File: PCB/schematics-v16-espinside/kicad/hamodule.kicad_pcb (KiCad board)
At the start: 2 copper layers, 76.7 x 84.3 mm, 77 parts, among them J1 2604-1104, J2 2604-1102, J3 USB_B_Micro, J4 ESP Relays, J5 Current Jumper, J6 GND 3.3V, J7 Conn_01x02, J8 Current Jumper, J9 2604-1104, K1 PCN-105D, K2 PCN-105D, K3 PCN-105D, K4 PCN-105D, Q1 2N2219, Q2 2N2219, SW1 EN, SW2 IO0, U1 ULN2003A, U2 ESP32-WROOM-32D, U3 CP2102N-A01-GQFN24, U4 LD1117AV33_TO220, U6 LDA210-PDIP, U7 LDA210-PDIP

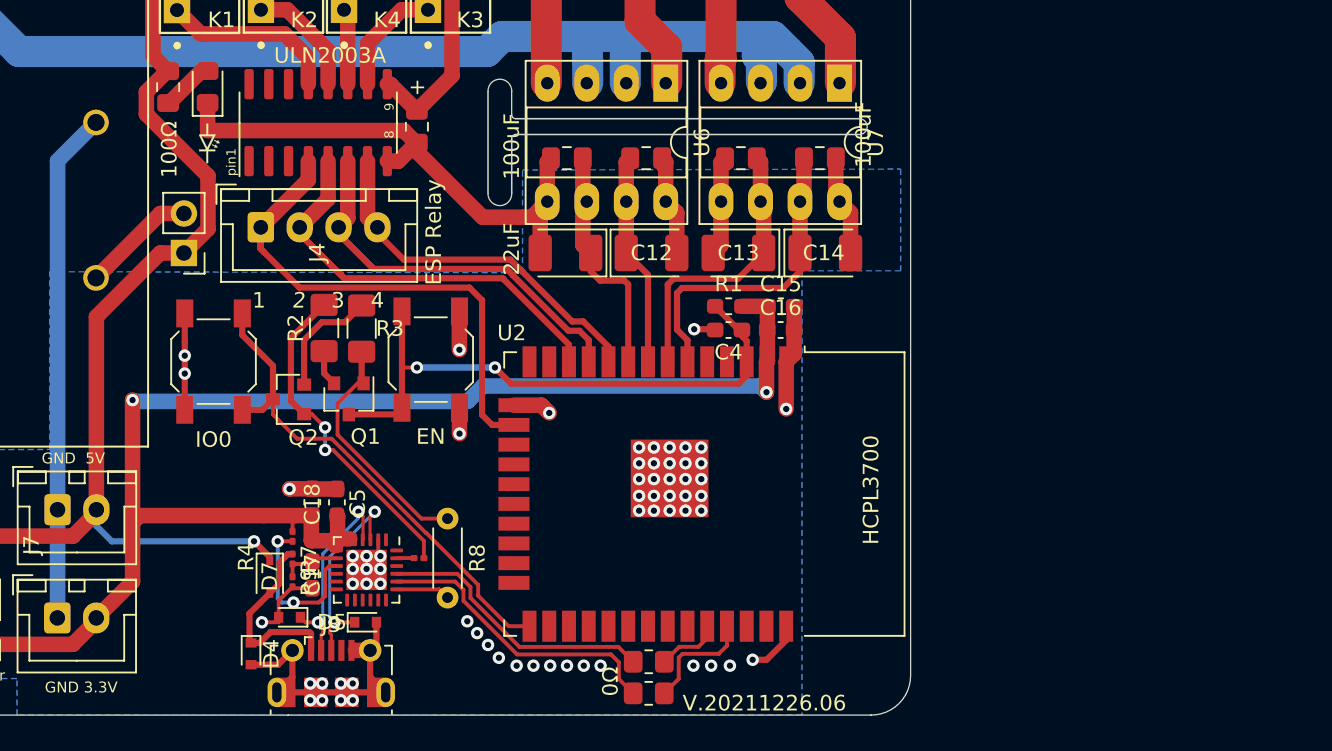
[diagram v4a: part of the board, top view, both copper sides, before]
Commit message: adding temp sensor + Serial pins
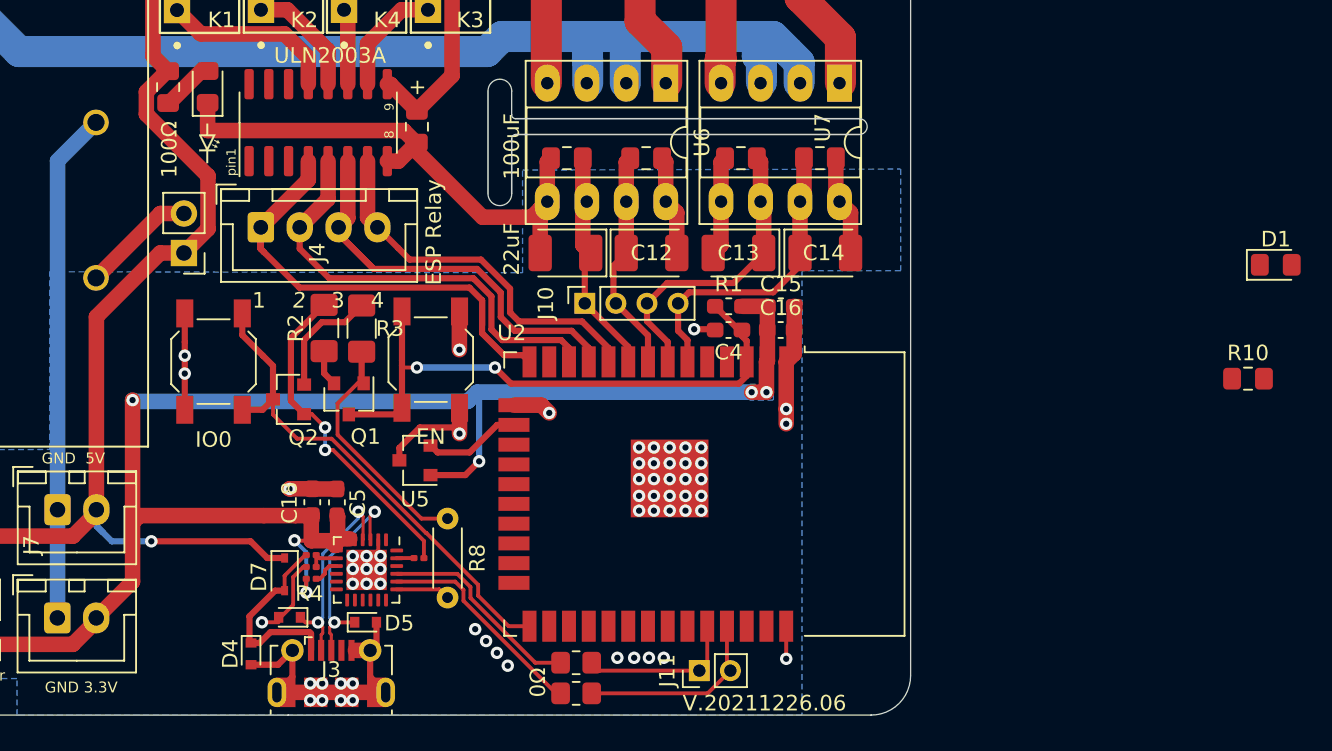
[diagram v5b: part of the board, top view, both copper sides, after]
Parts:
- removed C17: 100nF, Capacitor_SMD:C_0603_1608Metric_Pad1.08x0.95mm_HandSolder
- added D1: LED, LED_SMD:LED_0805_2012Metric_Pad1.15x1.40mm_HandSolder, F.Cu at (225.4, 122.7)
- added J10: EspSense, Connector_PinSocket_2.00mm:PinSocket_1x04_P2.00mm_Vertical, F.Cu at (180.9, 125.2)
- added J11: Conn_01x02_Male, Connector_PinHeader_2.00mm:PinHeader_1x02_P2.00mm_Vertical, F.Cu at (188.3, 148.8)
- added R10: 100Ω, Resistor_SMD:R_0805_2012Metric_Pad1.15x1.40mm_HandSolder, F.Cu at (223.6, 130.1)
- added U5: MCP9700T-ETT, Package_TO_SOT_SMD:SOT-23, F.Cu at (170.0, 135.3)
- moved R6 4.67 mm to (180.4, 148.3)
- moved R5 4.67 mm to (180.4, 150.3)
- moved R4 2.98 mm to (163.3, 142.9), turned to 180 degrees
- moved R9 1.54 mm to (163.3, 142.2), turned to 180 degrees
- moved R7 1.23 mm to (163.3, 141.4), turned to 0 degrees
- moved D7 0.97 mm to (161.6, 142.7)
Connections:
- U2 pad 14: (no net) -> EspRel4
- U2 pad 16: EspRel4 -> TempIn
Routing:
- net 3.3V+: track 90.9 -> 103.1 mm, vias 2 -> 6
- net Net-(R4-Pad1): track 10.5 -> 1.76 mm, vias 2 -> 0
- net TempIn: track 0.00 -> 6.28 mm
- net RXD0: track 4.15 -> 10.2 mm
- net Net-(R5-Pad2): track 19.2 -> 13.9 mm
- net TXD0: track 7.35 -> 12.5 mm
- net GND(5V): track 166.9 -> 171.9 mm, vias 65 -> 61
- net Net-(R6-Pad2): track 18.0 -> 13.3 mm
- net EspRel3: track 30.9 -> 28.5 mm
- net EspRel4: track 33.5 -> 35.6 mm
- net Net-(R7-Pad2): track 3.80 -> 2.15 mm
- net 5V+: track 107.1 -> 108.5 mm
- net EspSens3: track 18.3 -> 19.4 mm
- net EspSens4: track 20.6 -> 19.9 mm
- net EspSens2: track 13.8 -> 14.5 mm
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- added copper zone on B.Cu, net 3.3V+
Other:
- board text removed: "HCPL3700"

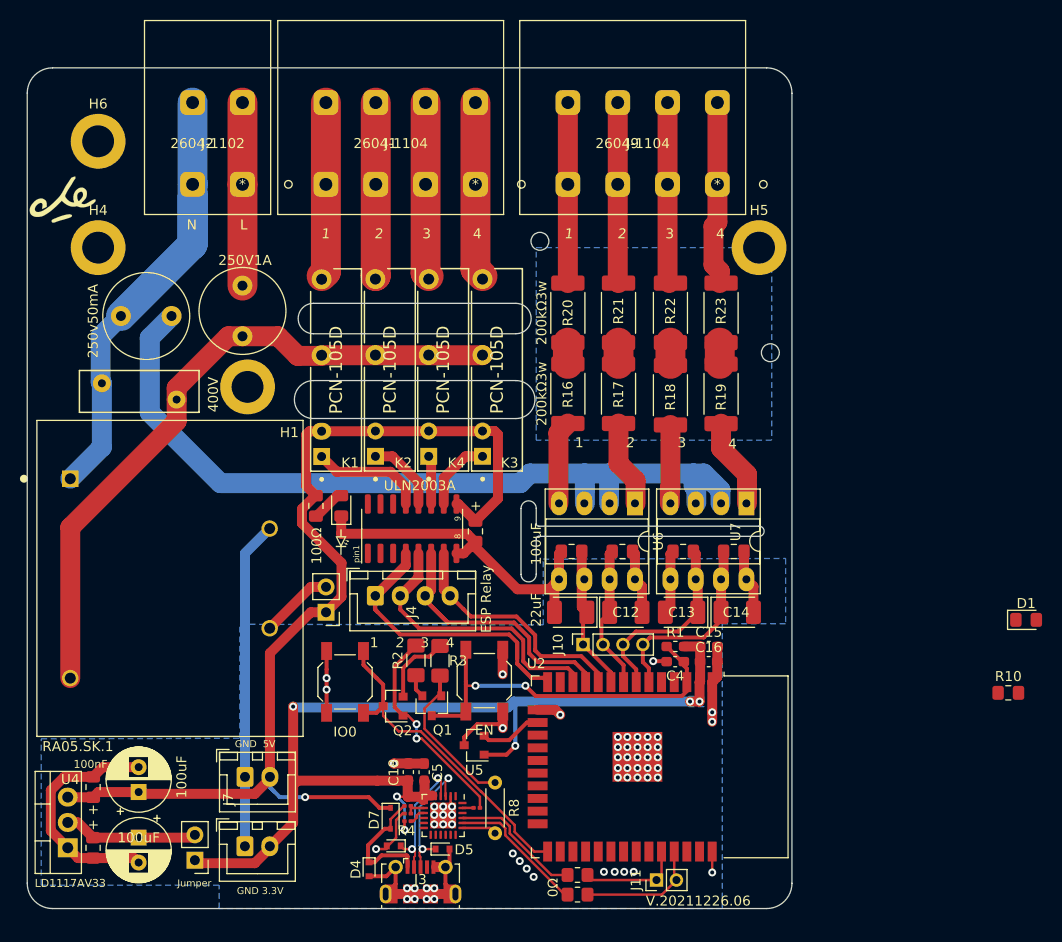
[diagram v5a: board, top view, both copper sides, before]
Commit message: updated part number
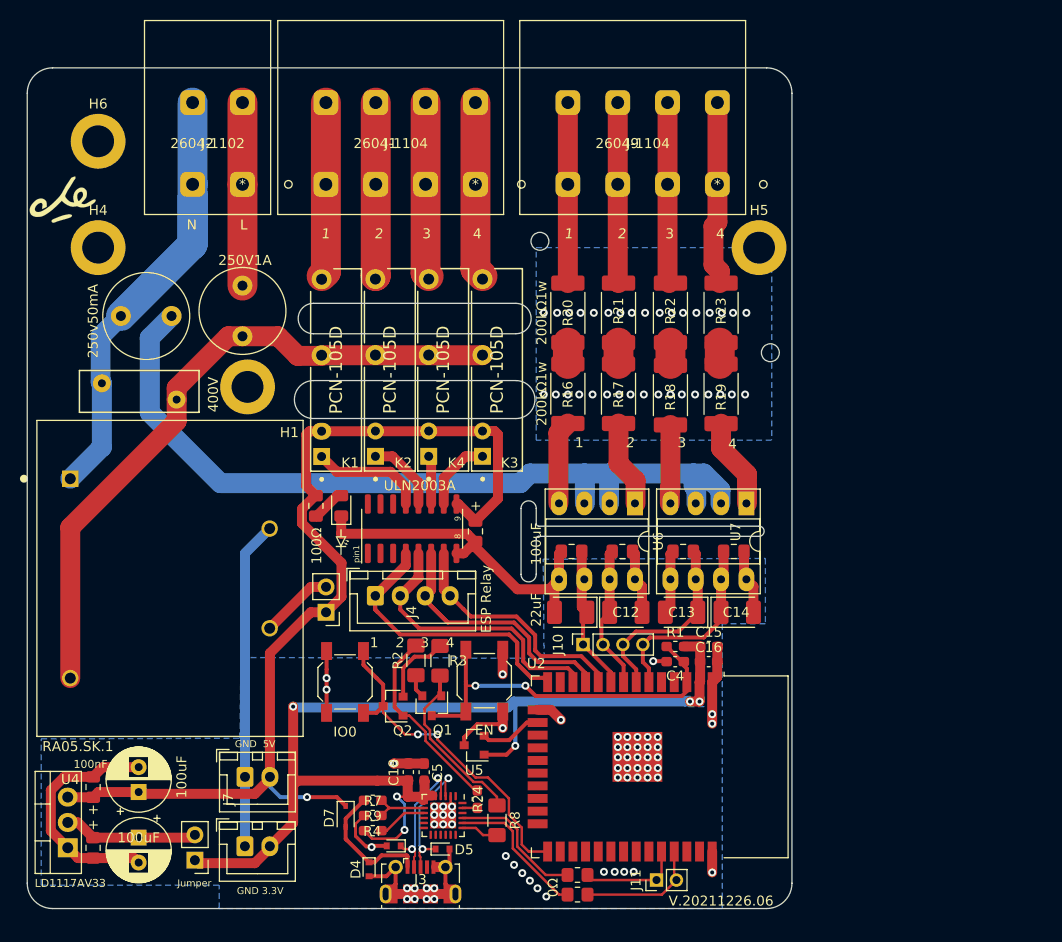
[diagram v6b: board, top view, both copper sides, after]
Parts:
- removed D1: LED, LED_SMD:LED_0805_2012Metric_Pad1.15x1.40mm_HandSolder
- removed R10: 100Ω, Resistor_SMD:R_0805_2012Metric_Pad1.15x1.40mm_HandSolder
- Q1, Q2: value 2N2219 -> SS8050
- R16, R17, R18, R19, R20, R21, R22, R23: value 200kΩ3w -> 200kΩ1w
- R24, R4, R7, R9: footprint Resistor_SMD:R_0201_0603Metric -> Resistor_SMD:R_0603_1608Metric_Pad1.05x0.95mm_HandSolder
- R8: footprint Resistor_THT:R_Axial_DIN0204_L3.6mm_D1.6mm_P5.08mm_Horizontal -> Resistor_SMD:R_1206_3216Metric_Pad1.42x1.75mm_HandSolder
- moved D7 4.51 mm to (157.1, 142.5)
- moved R8 3.79 mm to (172.3, 142.8)
- moved R4 3.63 mm to (159.8, 143.9)
- moved R7 3.55 mm to (159.8, 140.8)
- moved R9 3.51 mm to (159.8, 142.4)
- moved R24 0.88 mm to (170.3, 140.7), turned to 270 degrees
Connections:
- net GND(5V) renamed GND
- H5 pad 1: Net-(H5-Pad1) -> (no net)
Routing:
- net GND: track 171.9 -> 177.9 mm, vias 61 -> 62
- net 5V+: track 108.5 -> 103.3 mm
- net 3.3V+: track 103.1 -> 107.0 mm
- net Net-(R7-Pad2): track 2.15 -> 5.66 mm
- net Net-(R4-Pad1): track 1.76 -> 4.98 mm
- net DTR: track 21.3 -> 19.4 mm, vias 2 -> 0
- net RTS: track 15.6 -> 17.5 mm
- net IO0: track 32.1 -> 33.8 mm, vias 0 -> 2
- net Net-(R5-Pad2): track 13.9 -> 14.5 mm
- net Net-(R6-Pad2): track 13.3 -> 13.9 mm
- net (no net): vias 0 -> 35
- added copper zone on B.Cu, net (none)
- removed copper zone on B.Cu, net Net-(H5-Pad1)

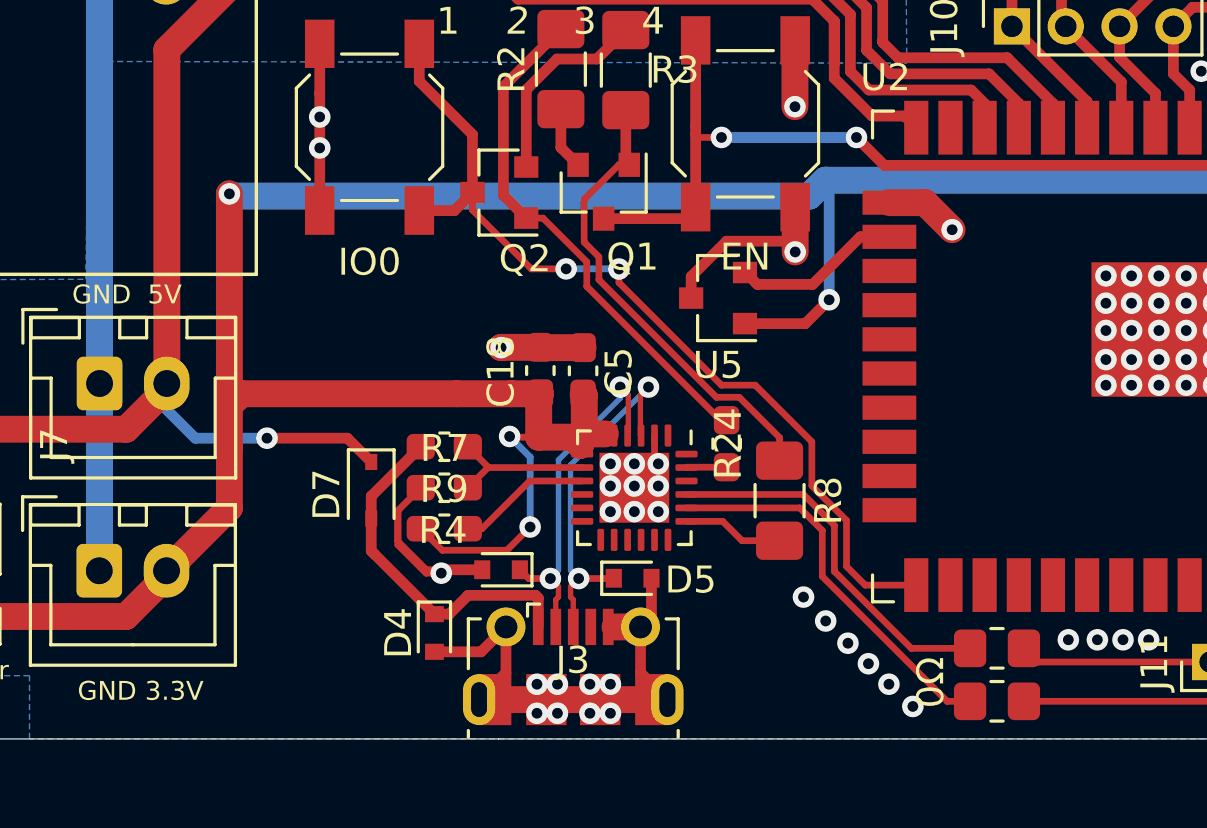
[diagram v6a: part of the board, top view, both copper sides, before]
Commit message: updated CP to same version as devkit + started working on BOM
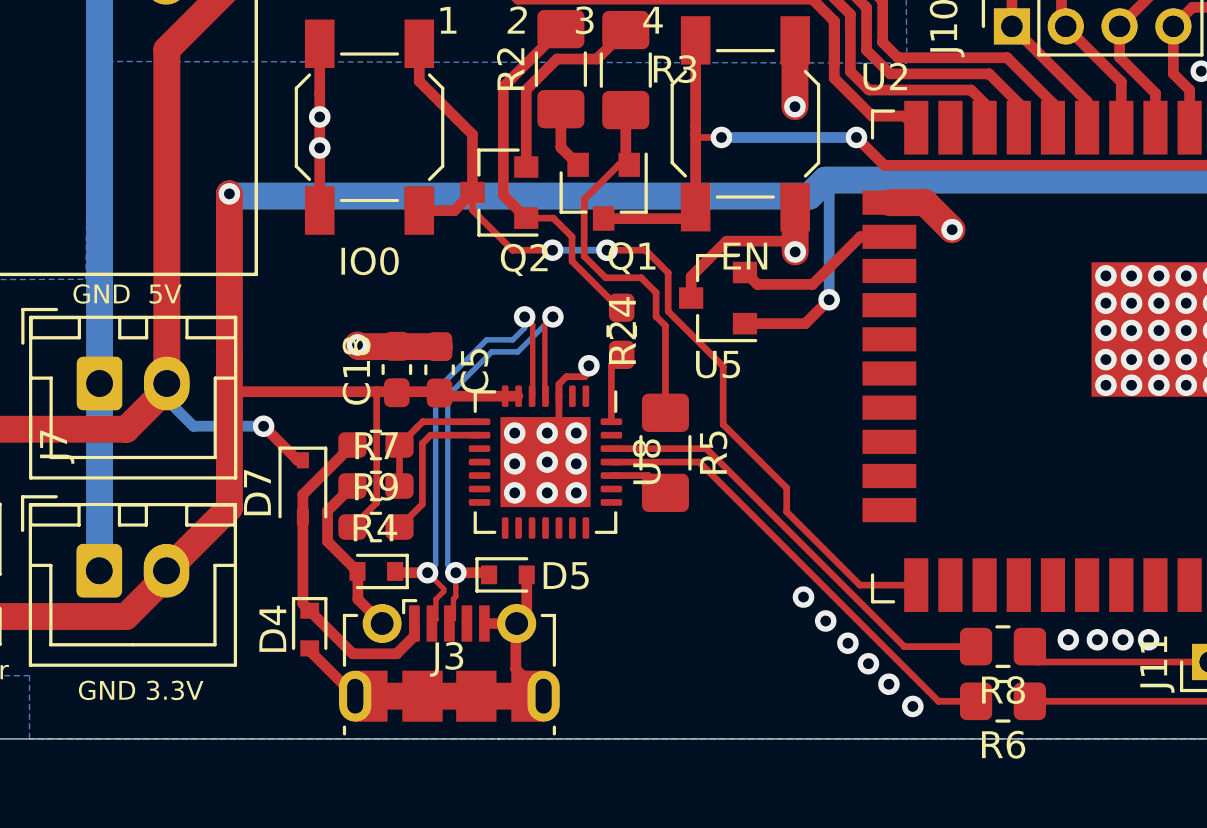
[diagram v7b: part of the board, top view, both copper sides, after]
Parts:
- removed U3: CP2102N-A01-GQFN24, Package_DFN_QFN:QFN-24-1EP_4x4mm_P0.5mm_EP2.6x2.6mm
- added U8: CP2102N-A01-GQFN28, Package_DFN_QFN:QFN-28-1EP_5x5mm_P0.5mm_EP3.35x3.35mm, F.Cu at (163.6, 141.4)
- R5: value 0Ω -> 1kΩ; footprint Resistor_SMD:R_0805_2012Metric_Pad1.20x1.40mm_HandSolder -> Resistor_SMD:R_1206_3216Metric_Pad1.42x1.75mm_HandSolder
- R8: value 1kΩ -> 0Ω; footprint Resistor_SMD:R_1206_3216Metric_Pad1.42x1.75mm_HandSolder -> Resistor_SMD:R_0805_2012Metric_Pad1.20x1.40mm_HandSolder
- moved R5 15.4 mm to (168.0, 141.1), turned to 270 degrees
- moved R8 9.92 mm to (180.6, 148.3), turned to 180 degrees
- moved R24 5.71 mm to (166.4, 136.6)
- moved C18 5.33 mm to (158.1, 138.0)
- moved C5 5.33 mm to (159.6, 138.0)
- moved D4 4.64 mm to (154.8, 147.6)
- moved D5 4.64 mm to (162.2, 145.6)
- moved D6 4.64 mm to (157.3, 145.5)
- moved J3 4.60 mm to (160.0, 148.9)
- moved D7 2.54 mm to (154.6, 142.4)
- moved R4 2.54 mm to (157.3, 143.8)
- moved R7 2.54 mm to (157.3, 140.8)
- moved R9 2.54 mm to (157.3, 142.3)
- moved R6 1.98 mm to (180.6, 150.3)
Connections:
- R5 pad 1: TXD0 -> RTS
- R6 pad 1: RXD0 -> TXD0
- R8 pad 1: RTS -> RXD0
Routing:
- net Net-(R8-Pad2): track 3.76 -> 16.6 mm
- net Net-(R5-Pad2): track 14.5 -> 2.27 mm
- net 3.3V+: track 107.0 -> 95.9 mm, vias 6 -> 4
- net D+: track 13.7 -> 19.5 mm
- net DTR: track 19.4 -> 13.7 mm
- net GND: track 177.9 -> 172.5 mm, vias 62 -> 55
- net D-: track 13.4 -> 18.4 mm
- net Net-(R6-Pad2): track 13.9 -> 17.2 mm
- net RTS: track 17.5 -> 14.2 mm
- net 5V+: track 103.3 -> 100.5 mm
- net Net-(R24-Pad2): track 1.12 -> 2.65 mm
- net VBUS: track 13.2 -> 12.3 mm
- net Net-(R7-Pad2): track 5.66 -> 4.86 mm
- net Net-(R4-Pad1): track 4.98 -> 5.71 mm
- net (no net): vias 35 -> 34

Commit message: new routing
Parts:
- added H2: MountingHole_Pad, MountingHole:MountingHole_2.2mm_M2_DIN965_Pad_TopOnly, B.Cu at (199.2, 103.3)
- added H3: MountingHole_Pad, MountingHole:MountingHole_2.2mm_M2_DIN965_Pad_TopOnly, B.Cu at (175.7, 84.9)
- C1, C2, C3: footprint Capacitor_SMD:C_0805_2012Metric_Pad1.15x1.40mm_HandSolder -> Capacitor_SMD:C_0603_1608Metric_Pad1.08x0.95mm_HandSolder
- C10, C7, C8, C9: value 100uF -> 100nF; footprint Capacitor_SMD:C_0805_2012Metric_Pad1.15x1.40mm_HandSolder -> Capacitor_SMD:C_0603_1608Metric_Pad1.08x0.95mm_HandSolder
- R2, R3: footprint Resistor_SMD:R_1206_3216Metric_Pad1.42x1.75mm_HandSolder -> Resistor_SMD:R_0603_1608Metric_Pad1.05x0.95mm_HandSolder
- moved G*** 6.55 mm to (163.5, 112.2)
- moved R3 2.67 mm to (163.9, 127.1), turned to 0 degrees
- moved U5 2.11 mm to (171.5, 136.8)
- moved R2 1.91 mm to (163.9, 128.7), turned to 180 degrees
- moved R24 0.81 mm to (165.6, 136.6)
- moved R18 0.14 mm to (189.7, 100.1)
- moved D6 0.14 mm to (157.4, 145.6)
- moved D5 0.13 mm to (162.1, 145.6)
- turned Q2 to 270 degrees
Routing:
- net GND: track 172.5 -> 195.4 mm, vias 55 -> 56
- net HeatPad: track 0.00 -> 15.5 mm, vias 0 -> 36
- net DTR: track 13.7 -> 8.43 mm
- net D+: track 19.5 -> 16.5 mm
- net Net-(Q2-Pad2): track 7.49 -> 4.94 mm
- net RTS: track 14.2 -> 16.2 mm
- net D-: track 18.4 -> 16.7 mm
- net IO0: track 34.1 -> 32.9 mm
- net TempIn: track 6.28 -> 5.08 mm
- net Net-(Q1-Pad2): track 2.33 -> 1.68 mm
- net EN: track 38.3 -> 38.4 mm, vias 2 -> 0
- net (no net): vias 34 -> 0
- added copper zone on B.Cu, net HeatPad
- removed copper zone on B.Cu, net (none)
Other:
- outline, holes or cut-outs redrawn
- board text added: "V.20211231.06"
- board text removed: "V.20211226.06"
